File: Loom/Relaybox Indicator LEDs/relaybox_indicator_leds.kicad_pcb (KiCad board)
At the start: 2 copper layers, 37 parts, among them J1 1-776276-1, J2 1-776276-1, SW1 SW_DPDT_x2, SW2 SW_DPDT_x2, SW3 SW_DPDT_x2, SW4 SW_DPDT_x2, SW5 SW_DPDT_x2, SW6 SW_DPDT_x2, SW7 SW_DPDT_x2

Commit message: PCB design
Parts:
- added G***: LOGO, relaybox_indicator_leds:FBR_logo_for_PCB_25mm, F.Cu at (41.6, 81.6)
- added REF**: MountingHole_3.2mm_M3_Pad, MountingHole:MountingHole_3.2mm_M3_Pad, F.Cu at (153.3, 36.3)
- added REF**: MountingHole_3.2mm_M3_Pad, MountingHole:MountingHole_3.2mm_M3_Pad, F.Cu at (153.3, 127.0)
- added REF**: MountingHole_3.2mm_M3_Pad, MountingHole:MountingHole_3.2mm_M3_Pad, F.Cu at (31.2, 127.0)
- added REF**: MountingHole_3.2mm_M3_Pad, MountingHole:MountingHole_3.2mm_M3_Pad, F.Cu at (31.2, 36.3)
- added TP1: TestPoint, TestPoint:TestPoint_THTPad_D3.0mm_Drill1.5mm, F.Cu at (77.2, 50.2)
- added TP10: TestPoint, TestPoint:TestPoint_THTPad_D3.0mm_Drill1.5mm, F.Cu at (101.2, 85.9)
- added TP11: TestPoint, TestPoint:TestPoint_THTPad_D3.0mm_Drill1.5mm, F.Cu at (113.2, 85.9)
- added TP12: TestPoint, TestPoint:TestPoint_THTPad_D3.0mm_Drill1.5mm, F.Cu at (125.2, 85.9)
- added TP13: TestPoint, TestPoint:TestPoint_THTPad_D3.0mm_Drill1.5mm, F.Cu at (137.2, 85.9)
- added TP14: TestPoint, TestPoint:TestPoint_THTPad_D3.0mm_Drill1.5mm, F.Cu at (149.2, 85.9)
- added TP15: TestPoint, TestPoint:TestPoint_THTPad_D3.0mm_Drill1.5mm, F.Cu at (149.2, 78.4)
- added TP2: TestPoint, TestPoint:TestPoint_THTPad_D3.0mm_Drill1.5mm, F.Cu at (89.2, 50.2)
- added TP3: TestPoint, TestPoint:TestPoint_THTPad_D3.0mm_Drill1.5mm, F.Cu at (101.2, 50.2)
- added TP4: TestPoint, TestPoint:TestPoint_THTPad_D3.0mm_Drill1.5mm, F.Cu at (113.2, 50.2)
- added TP5: TestPoint, TestPoint:TestPoint_THTPad_D3.0mm_Drill1.5mm, F.Cu at (125.2, 50.2)
- added TP6: TestPoint, TestPoint:TestPoint_THTPad_D3.0mm_Drill1.5mm, F.Cu at (137.2, 50.2)
- added TP7: TestPoint, TestPoint:TestPoint_THTPad_D3.0mm_Drill1.5mm, F.Cu at (149.2, 50.2)
- added TP8: TestPoint, TestPoint:TestPoint_THTPad_D3.0mm_Drill1.5mm, F.Cu at (77.2, 85.9)
- added TP9: TestPoint, TestPoint:TestPoint_THTPad_D3.0mm_Drill1.5mm, F.Cu at (89.2, 85.9)
- moved R14 66.6 mm to (149.2, 101.3)
- moved D14 65.8 mm to (149.2, 118.5)
- moved R13 61.8 mm to (137.2, 101.3)
- moved D13 61.4 mm to (137.2, 118.5)
- moved R12 59.8 mm to (125.2, 101.1)
- moved D12 59.3 mm to (125.2, 118.5)
- moved R11 57.4 mm to (113.2, 101.3)
- moved SW7 56.6 mm to (145.8, 98.4)
- moved D11 56.5 mm to (113.2, 118.5)
- moved SW6 53.6 mm to (133.8, 98.4)
- moved SW5 52.2 mm to (121.8, 98.4)
- moved R10 51.7 mm to (101.2, 101.1)
- moved D10 49.5 mm to (101.2, 118.5)
- moved SW4 48.6 mm to (109.8, 98.4)
- moved R9 45.7 mm to (89.2, 101.1)
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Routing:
- net /+12V: track 0.00 -> 344.6 mm
- net /GND: track 137.3 -> 0.00 mm
- net /SIG7: track 0.00 -> 134.6 mm
- net /SIG6: track 0.00 -> 117.6 mm
- net /POW7: track 0.00 -> 113.8 mm
- net /SIG5: track 0.00 -> 113.2 mm
- net /POW6: track 0.00 -> 97.0 mm
- net /SIG4: track 0.00 -> 96.2 mm
- net /SIG3: track 0.00 -> 92.7 mm
- net /POW5: track 0.00 -> 91.8 mm
- net /SIG2: track 0.00 -> 75.3 mm
- net /POW4: track 0.00 -> 75.0 mm
- net /POW3: track 1.59 -> 69.8 mm
- net /SIG1: track 111.8 -> 57.9 mm
- net /POW2: track 0.00 -> 53.0 mm
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- added copper zone on F.Cu, net (none)
- added copper zone on B.Cu, net /GND
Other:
- board outline added: 132.1 x 100.7 mm

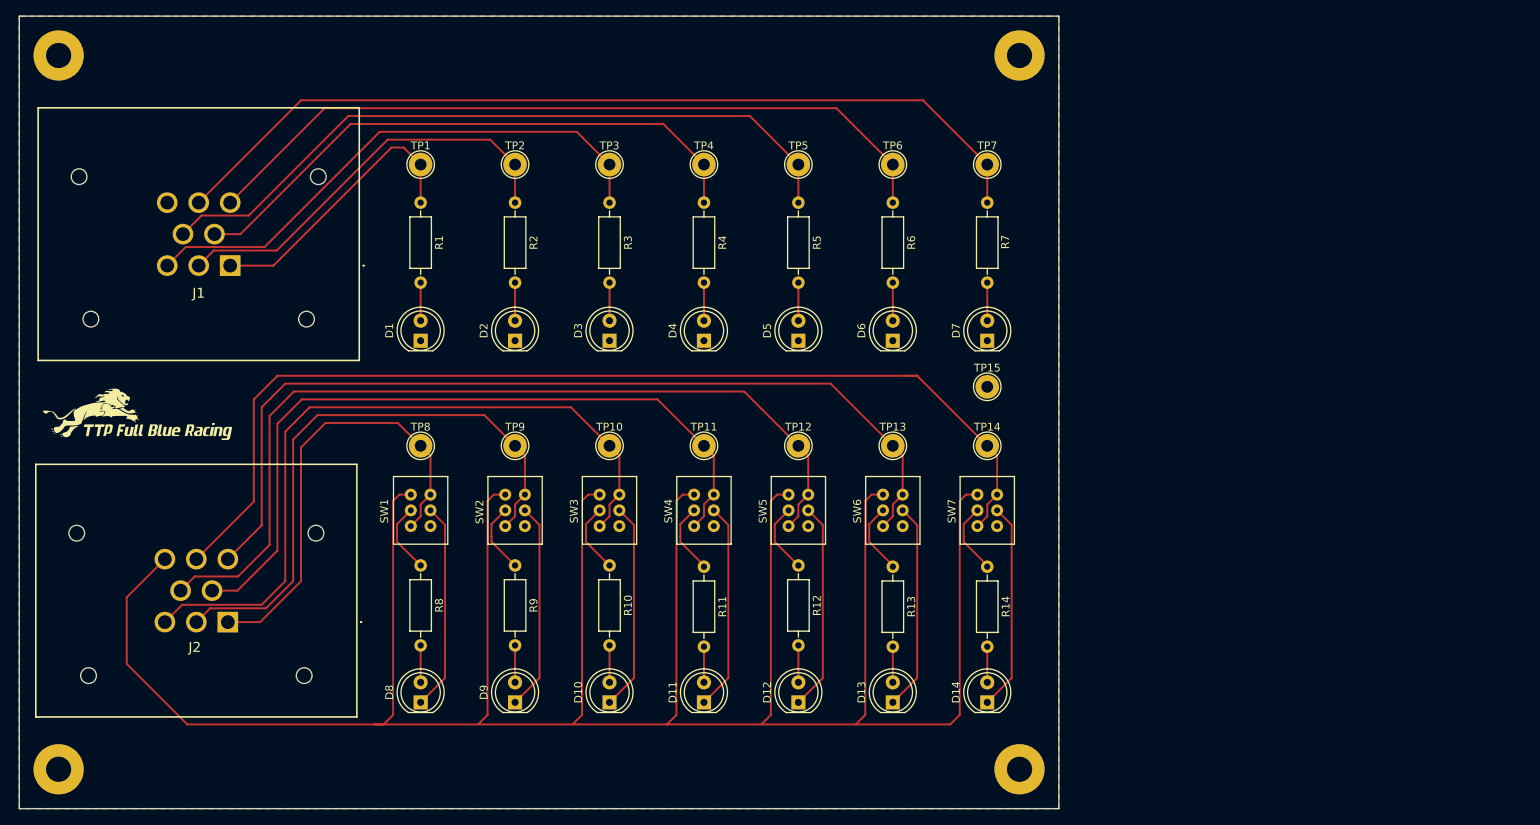
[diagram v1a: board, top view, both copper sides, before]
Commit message: Removed islands and added rounded corners
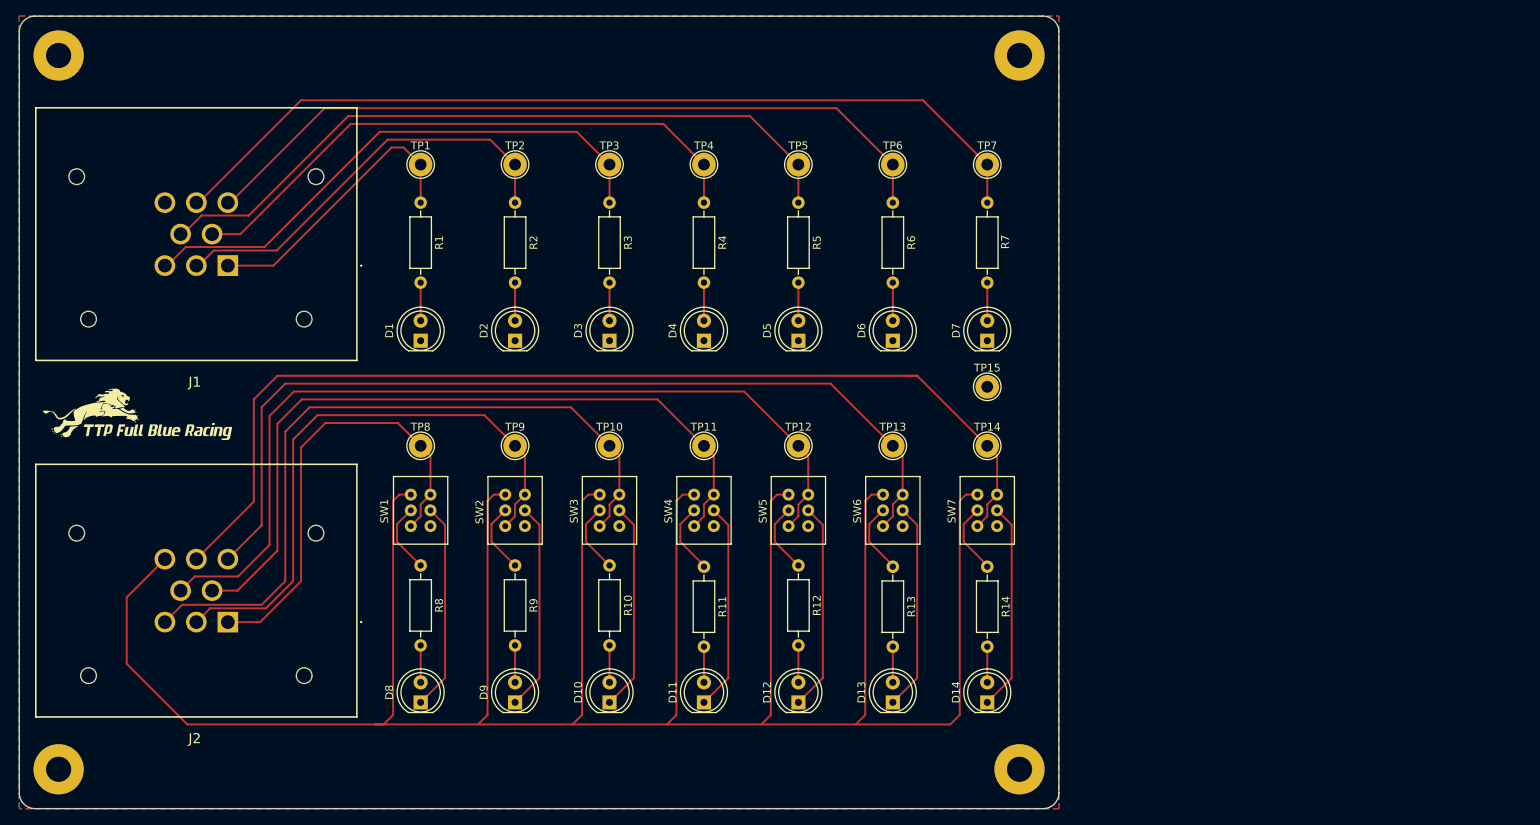
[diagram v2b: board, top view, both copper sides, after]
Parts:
- moved J1 0.30 mm to (52.7, 63.0)
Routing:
- added copper zone on F.Cu, net /GND
- removed copper zone on F.Cu, net (none)
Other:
- outline, holes or cut-outs redrawn
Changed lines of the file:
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@@
   )
   (footprint "relaybox_indicator_leds:17762761" (layer "F.Cu")
-    (at 53 63 180)
+    (at 52.7 63 180)
     (descr "1-776276-1-2")
     (tags "Connector")
@@
     (property "ki_description" "PCB Mount Header, Vertical, Wire-to-Board, 8 Position, 4 mm [.157 in] Centerline, Fully Shrouded, Gold, Through Hole - Solder, Sealable, AMPSEAL")
     (attr through_hole)
-    (fp_text reference "J1" (at 4 -3.5) (layer "F.SilkS")
+    (fp_text reference "J1" (at 4.2 -14.8) (layer "F.SilkS")
         (effects (font (size 1.27 1.27) (thickness 0.254)))
     )
@@
     (property "ki_description" "PCB Mount Header, Vertical, Wire-to-Board, 8 Position, 4 mm [.157 in] Centerline, Fully Shrouded, Gold, Through Hole - Solder, Sealable, AMPSEAL")
     (attr through_hole)
-    (fp_text reference "J2" (at 4.2 -3.2) (layer "F.SilkS")
+    (fp_text reference "J2" (at 4.2 -14.8) (layer "F.SilkS")
         (effects (font (size 1.27 1.27) (thickness 0.254)))
     )
@@
     )
   )
-  (gr_rect (start 26.2 31.3) (end 158.3 132)
-    (stroke (width 0.1) (type default)) (fill none) (layer "Edge.Cuts"))
+  (gr_arc (start 156.3 31.3) (mid 157.714214 31.885786) (end 158.3 33.3)
+    (stroke (width 0.1) (type default)) (layer "Edge.Cuts"))
+  (gr_line (start 26.200001 129.999999) (end 26.2 33.3)
+    (stroke (width 0.1) (type default)) (layer "Edge.Cuts"))
+  (gr_arc (start 26.2 33.3) (mid 26.785786 31.885786) (end 28.2 31.3)
+    (stroke (width 0.1) (type default)) (layer "Edge.Cuts"))
+  (gr_arc (start 28.200001 131.999999) (mid 26.785787 131.414213) (end 26.200001 129.999999)
+    (stroke (width 0.1) (type default)) (layer "Edge.Cuts"))
+  (gr_arc (start 158.299999 129.999999) (mid 157.714213 131.414213) (end 156.299999 131.999999)
+    (stroke (width 0.1) (type default)) (layer "Edge.Cuts"))
+  (gr_line (start 158.3 33.3) (end 158.299999 129.999999)
+    (stroke (width 0.1) (type default)) (layer "Edge.Cuts"))
+  (gr_line (start 28.2 31.3) (end 156.3 31.3)
+    (stroke (width 0.1) (type default)) (layer "Edge.Cuts"))
+  (gr_line (start 156.299999 131.999999) (end 28.200001 131.999999)
+    (stroke (width 0.1) (type default)) (layer "Edge.Cuts"))
   (segment (start 77.2 65.16) (end 77.2 70) (width 0.25) (layer "F.Cu") (net 2))
   (segment (start 89.2 65.16) (end 89.2 70) (width 0.25) (layer "F.Cu") (net 3))
@@
   (segment (start 149.2 101.1) (end 146.2 98.1) (width 0.25) (layer "F.Cu") (net 44))
   (segment (start 146.2 95.85) (end 146.2 97.4) (width 0.25) (layer "F.Cu") (net 44))
-  (zone (net 0) (net_name "") (layer "F.Cu") (hatch edge 0.5)
+  (zone (net 1) (net_name "/GND") (layers "F&B.Cu") (hatch edge 0.5)
     (priority 1)
     (connect_pads (clearance 0.5))
     (min_thickness 0.25) (filled_areas_thickness no)
-    (fill yes (thermal_gap 0.5) (thermal_bridge_width 0.5) (island_removal_mode 1) (island_area_min 1))
-    (polygon
-      (pts
-        (xy 26.2 31.3)
-        (xy 158.3 31.3)
-        (xy 158.3 132)
-        (xy 26.2 132)
-      )
-    )
-  )
-  (zone (net 1) (net_name "/GND") (layer "B.Cu") (hatch edge 0.5)
-    (connect_pads (clearance 0.5))
-    (min_thickness 0.25) (filled_areas_thickness no)
-    (fill yes (thermal_gap 0.5) (thermal_bridge_width 0.5) (island_removal_mode 1) (island_area_min 1))
+    (fill yes (thermal_gap 0.5) (thermal_bridge_width 0.5) (island_removal_mode 2) (island_area_min 1))
     (polygon
       (pts
